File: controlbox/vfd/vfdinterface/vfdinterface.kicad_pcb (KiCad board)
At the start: 2 copper layers, 29.7 x 22.7 mm, 13 parts, among them J1 Conn_01x04, J2 Conn_01x03, J3 Conn_01x02, Q2 BSS138, U1 TLC271ACP

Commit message: Route.
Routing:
- net GND: track 0.00 -> 66.5 mm
- net Net-(J1-Pin_2): track 0.00 -> 33.0 mm
- net +12V: track 0.00 -> 32.9 mm, vias 0 -> 1
- net Net-(J1-Pin_1): track 0.00 -> 29.7 mm
- net Net-(J1-Pin_3): track 0.00 -> 28.4 mm, vias 0 -> 1
- net Net-(U1-+): track 0.00 -> 15.8 mm
- net Net-(D1-A): track 0.00 -> 15.3 mm
- net Net-(J2-Pin_3): track 0.00 -> 5.86 mm
- net Net-(Q2-G): track 0.00 -> 5.79 mm
- net Relay: track 0.00 -> 5.53 mm

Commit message: Finish routing.
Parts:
- removed Q2: BSS138, Package_TO_SOT_SMD_AKL:SOT-23
- added Q1: BSS138, Package_TO_SOT_SMD_AKL:SOT-23, F.Cu at (66.7, 62.2)
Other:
- board text added: "+"

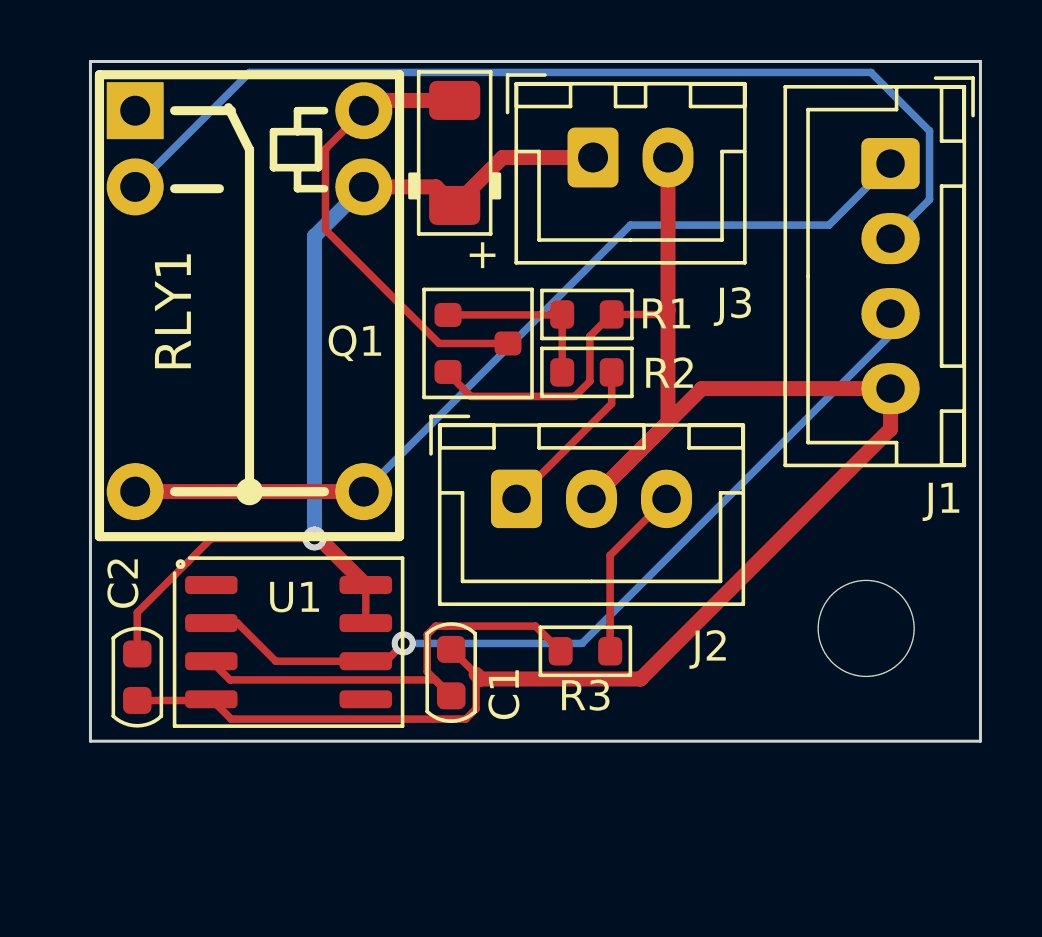
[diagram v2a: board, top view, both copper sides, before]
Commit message: Add fills.
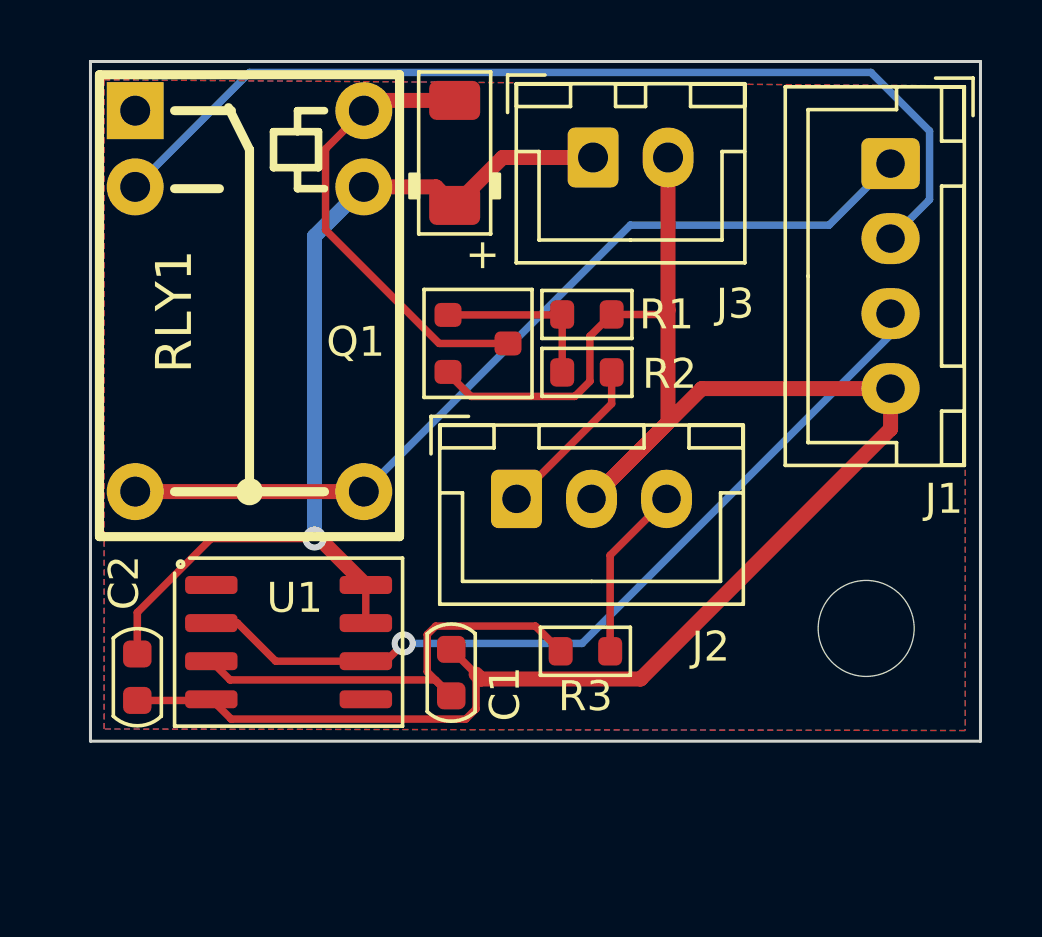
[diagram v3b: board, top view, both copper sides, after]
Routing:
- added copper zone on B.Cu, net (none)
- added copper zone on F.Cu, net (none)
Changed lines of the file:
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@@
 			(drillshape 0)
 			(scaleselection 1)
-			(outputdirectory "")
+			(outputdirectory "gerber/")
 		)
 	)
@@
 		(net 10)
 	)
+	(zone
+		(net 0)
+		(net_name "")
+		(layers "F&B.Cu")
+		(hatch edge 0.5)
+		(connect_pads
+			(clearance 0.5)
+		)
+		(min_thickness 0.25)
+		(filled_areas_thickness no)
+		(fill yes
+			(thermal_gap 0.5)
+			(thermal_bridge_width 0.5)
+			(island_removal_mode 1)
+			(island_area_min 10)
+		)
+		(polygon
+			(pts
+				(xy 54.2036 53.3908) (xy 82.9056 53.594) (xy 82.9056 75.0824) (xy 54.2036 75.0316)
+			)
+		)
+	)
 )

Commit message: Fix opamp gain.
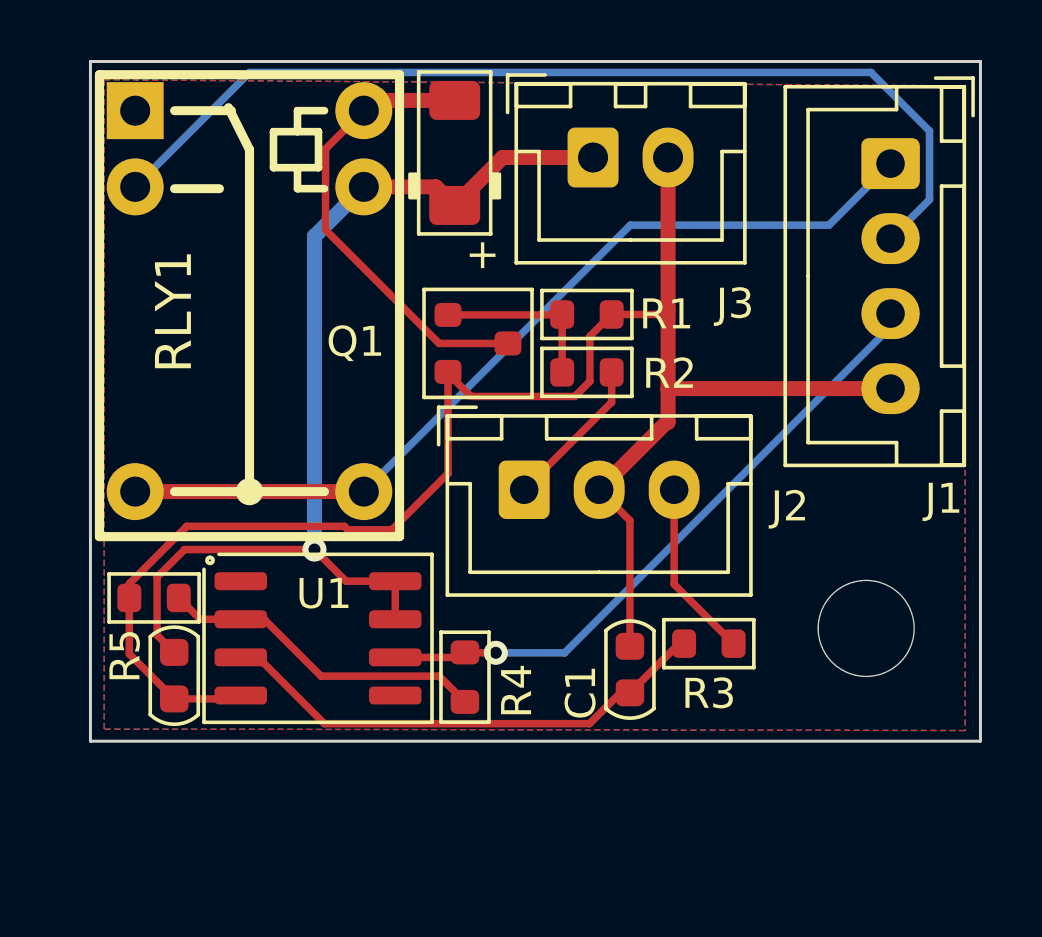
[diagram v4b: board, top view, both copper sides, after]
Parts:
- added R4: 51k, Resistor_SMD_AKL:R_0603_1608Metric, F.Cu at (66.2, 73.3)
- added R5: 22k, Resistor_SMD_AKL:R_0603_1608Metric, F.Cu at (55.9, 70.7)
- moved C1 5.96 mm to (71.7, 73.1)
- moved R3 4.12 mm to (74.4, 72.2)
- moved C2 1.23 mm to (56.5, 73.3)
- moved U1 0.99 mm to (61.3, 72.0)
- moved J2 0.40 mm to (68.2, 67.1)
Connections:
- U1 pad 2: Net-(J1-Pin_3) -> Net-(U1--)
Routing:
- net Net-(U1--): track 0.00 -> 11.0 mm
- net GND: track 66.5 -> 57.3 mm
- net Net-(J1-Pin_3): track 28.4 -> 22.2 mm
- net +12V: track 32.9 -> 34.1 mm
- net Net-(U1-+): track 15.8 -> 16.8 mm

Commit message: Change to DIL package.
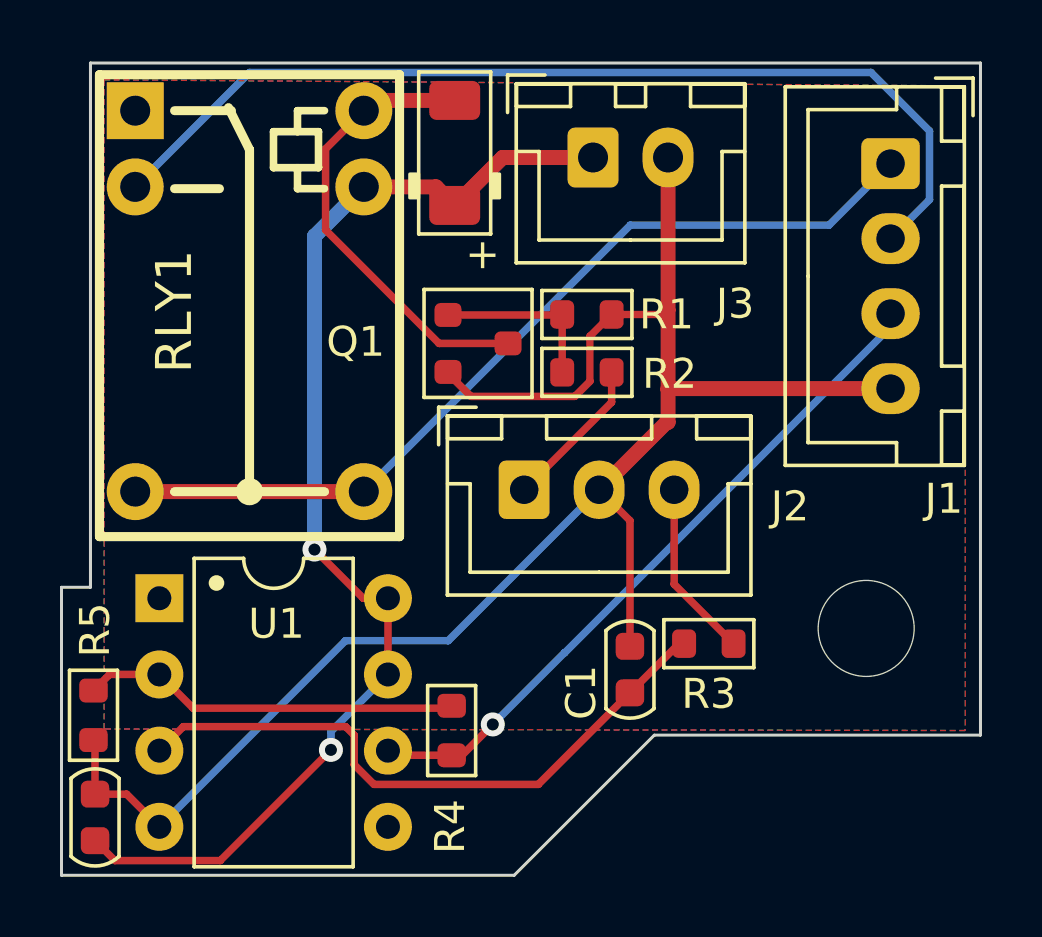
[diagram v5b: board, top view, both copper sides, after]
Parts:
- U1: footprint Package_SO_AKL:SO-8_3.9x4.9mm_P1.27mm -> Package_DIP_AKL:DIP-8_W7.62mm
- moved U1 5.46 mm to (56.0, 70.7)
- moved C2 5.41 mm to (53.9, 78.0), turned to 90 degrees
- moved R5 4.40 mm to (53.8, 74.6), turned to 90 degrees
- moved R4 1.83 mm to (65.8, 75.1), turned to -90 degrees
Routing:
- net +12V: track 34.1 -> 40.0 mm, vias 1 -> 2
- net Net-(U1-+): track 16.8 -> 21.5 mm
- net Net-(U1--): track 11.0 -> 12.6 mm
- net Net-(J1-Pin_3): track 22.2 -> 23.9 mm
- net GND: track 57.3 -> 58.5 mm
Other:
- board size 29.7 x 22.7 mm -> 30.6 x 27.1 mm
